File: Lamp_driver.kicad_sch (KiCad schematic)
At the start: 121 parts, among them J302 T44007, J303 T44007, J304 10146581-060_M, J305 T44007, J306 T44007, Q100 MDT7N65, Q301 MPF3N150, Q303 IXYH55N120, Q304 IXYH55N120, Q305 IXYH55N120, U301 IRS2184

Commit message: New placement strategy
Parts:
- R324: footprint Resistor_THT:R_Axial_DIN0617_L17.0mm_D6.0mm_P5.08mm_Vertical -> Resistor_THT:R_Axial_DIN0617_L17.0mm_D6.0mm_P20.32mm_Horizontal
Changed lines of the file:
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@@
 			(justify right bottom)
 		)
-		(property "Netclass" "400V"
+		(property "Netclass" "300V"
 			(at 197.485 172.8555 0)
 			(effects
@@
 			(justify right bottom)
 		)
-		(property "Netclass" "400V"
+		(property "Netclass" "300V"
 			(at 215.9 180.975 0)
 			(effects
@@
 			(justify right bottom)
 		)
-		(property "Netclass" "400V"
+		(property "Netclass" "300V"
 			(at 243.84 180.975 0)
 			(effects
@@
 			(justify right bottom)
 		)
-		(property "Netclass" "400V"
+		(property "Netclass" "300V"
 			(at 255.905 189.23 0)
 			(effects
@@
 			)
 		)
-		(property "Footprint" "Resistor_THT:R_Axial_DIN0617_L17.0mm_D6.0mm_P5.08mm_Vertical"
+		(property "Footprint" "Resistor_THT:R_Axial_DIN0617_L17.0mm_D6.0mm_P20.32mm_Horizontal"
 			(at 250.952 160.02 90)
 			(effects

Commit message: TP placement candidate 90%
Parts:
- R324: footprint Resistor_THT:R_Axial_DIN0617_L17.0mm_D6.0mm_P20.32mm_Horizontal -> Resistor_THT:R_Axial_DIN0617_L17.0mm_D6.0mm_P7.62mm_Vertical
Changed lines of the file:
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@@
 			)
 		)
-		(property "Footprint" "Resistor_THT:R_Axial_DIN0617_L17.0mm_D6.0mm_P20.32mm_Horizontal"
+		(property "Footprint" "Resistor_THT:R_Axial_DIN0617_L17.0mm_D6.0mm_P7.62mm_Vertical"
 			(at 250.952 160.02 90)
 			(effects

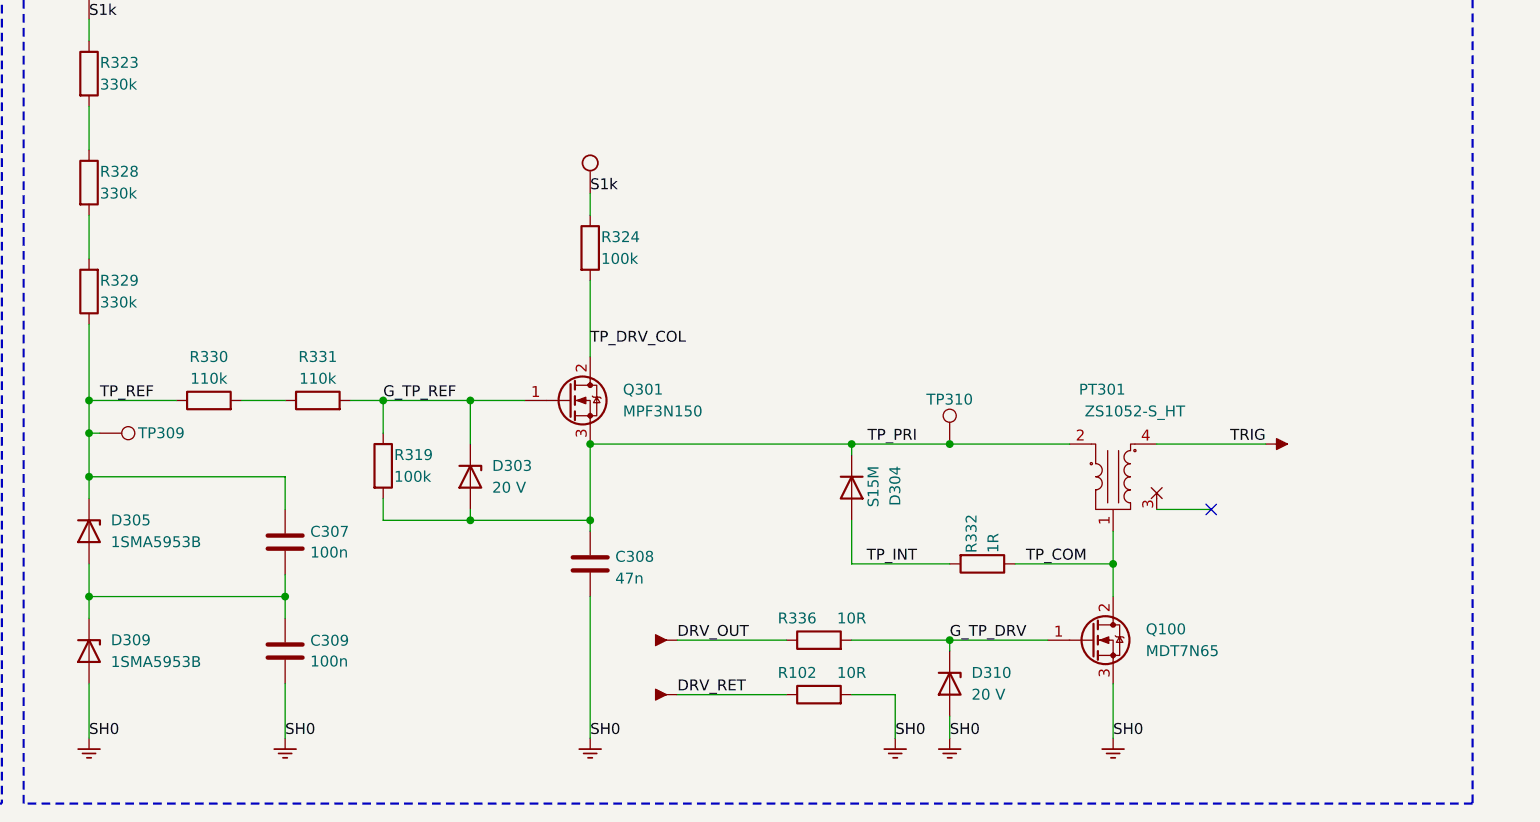
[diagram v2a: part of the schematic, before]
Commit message: Updated some clearance rules
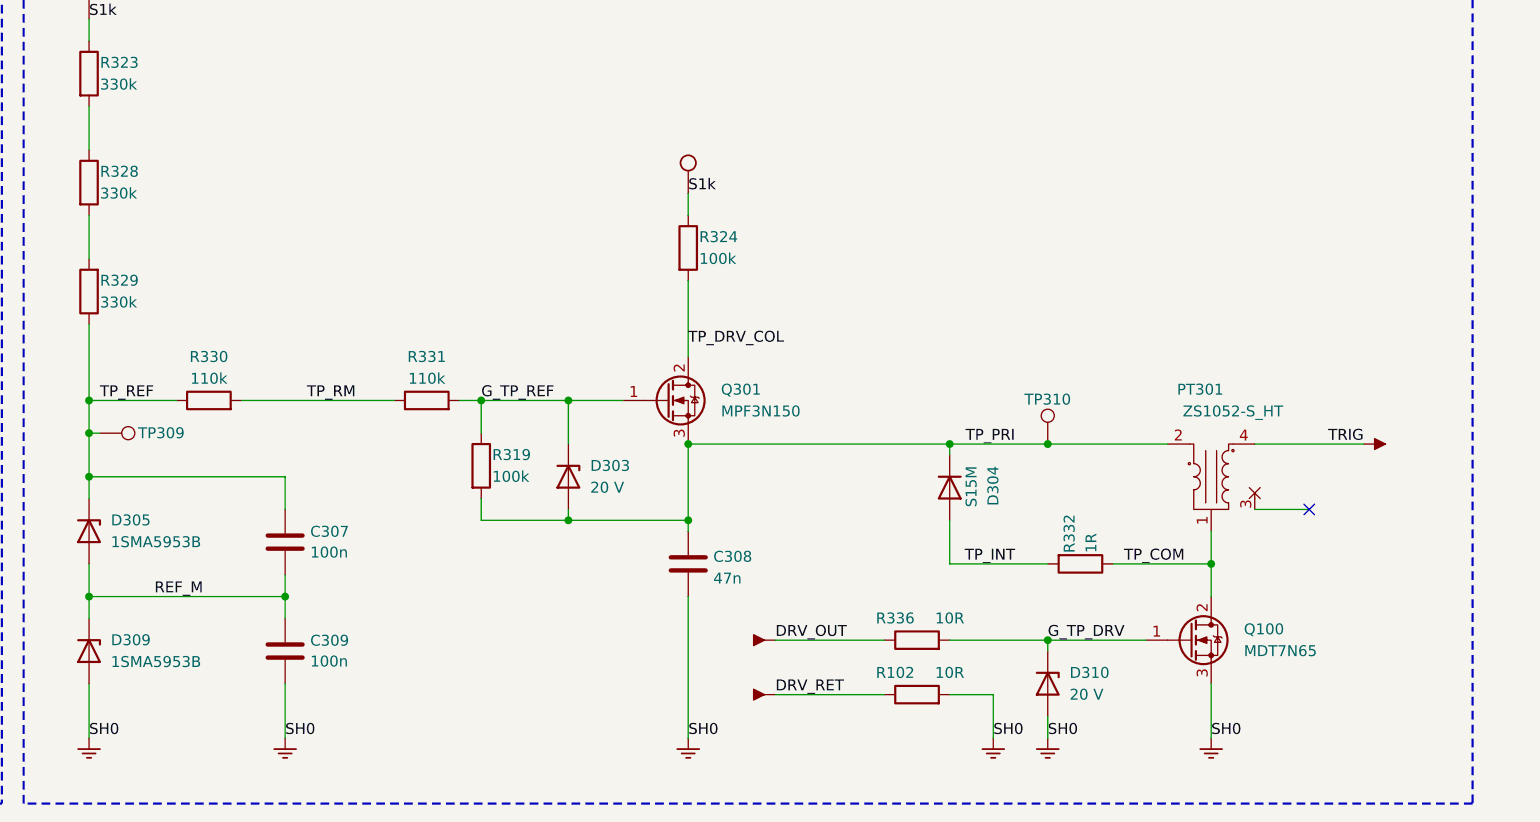
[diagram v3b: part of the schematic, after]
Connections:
- net TP_RM: now reaches R330.2, R331.1
- net REF_M: now reaches C307.2, C309.1, D305.2 (A), D309.1 (K)
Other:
- moved on the sheet: C308, D303, D304, D310, PT301, Q100, Q301, R102, R319, R324, R331, R332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

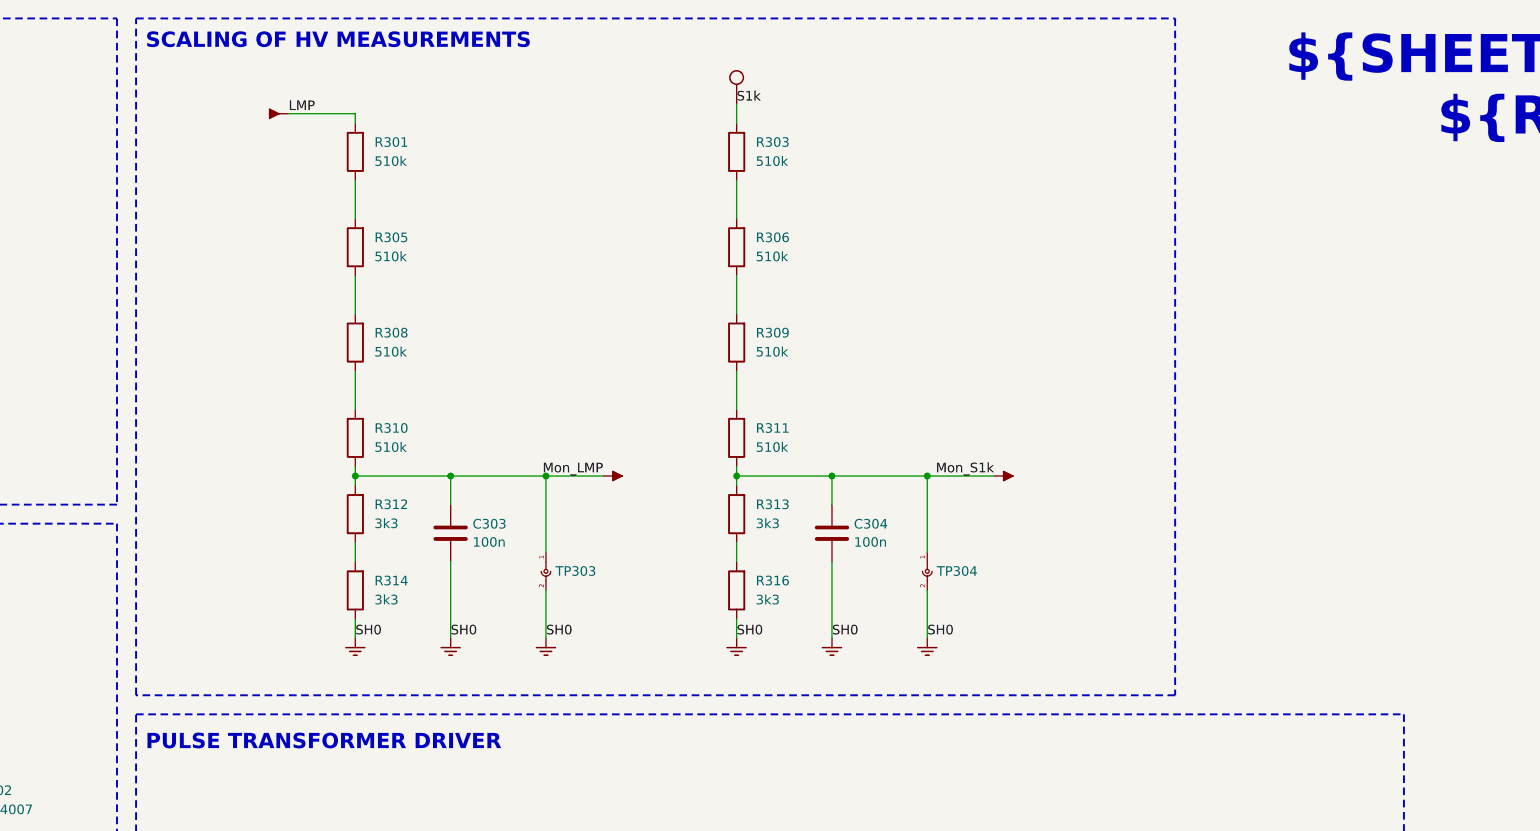
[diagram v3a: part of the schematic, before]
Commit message: Placement complplete, feasibility routing complete
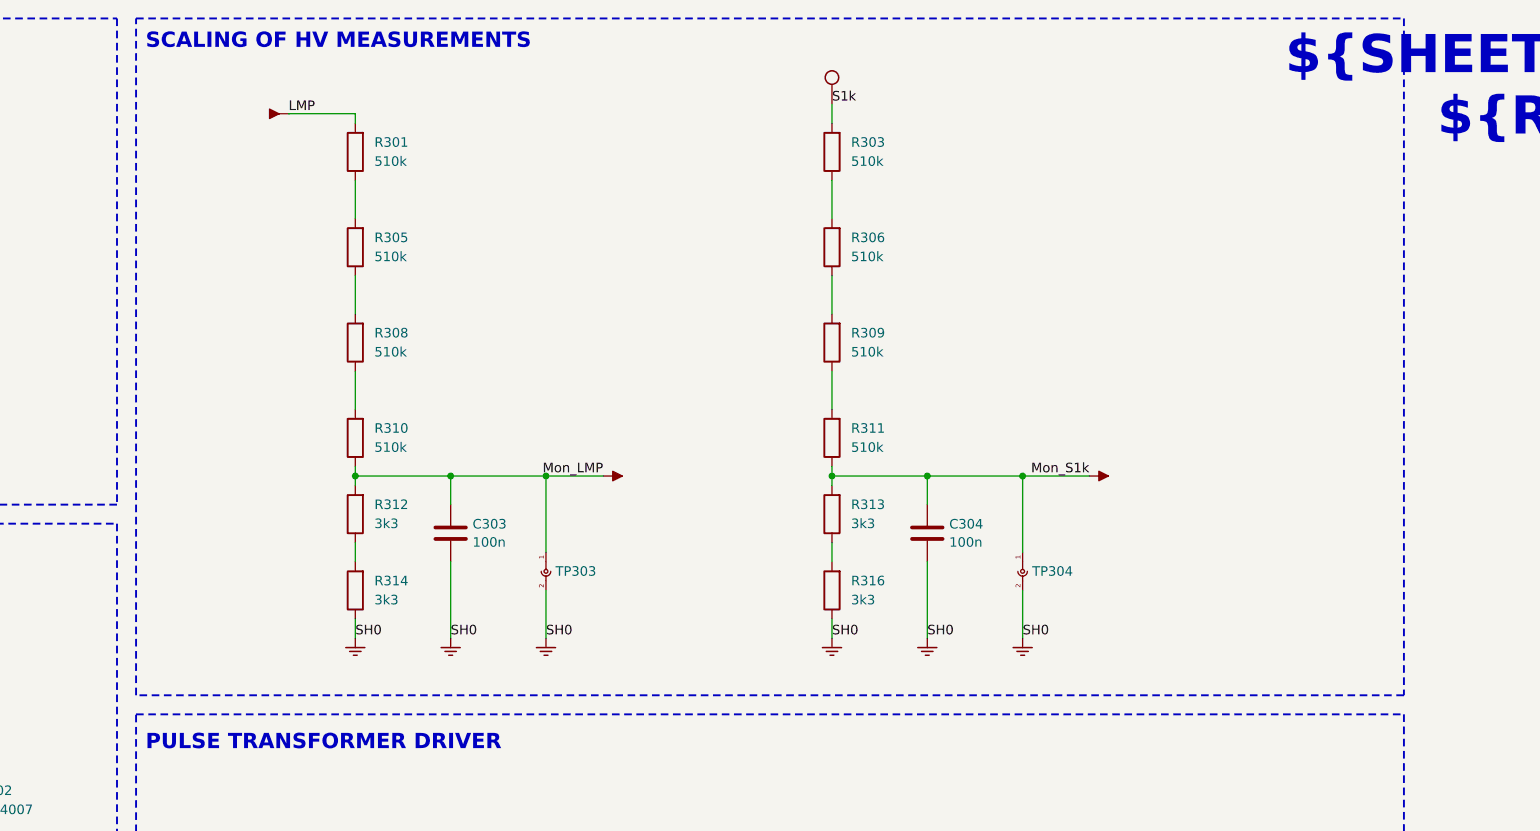
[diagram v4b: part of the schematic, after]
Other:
- moved on the sheet: C304, R303, R306, R309, R311, R313, R316, TP304

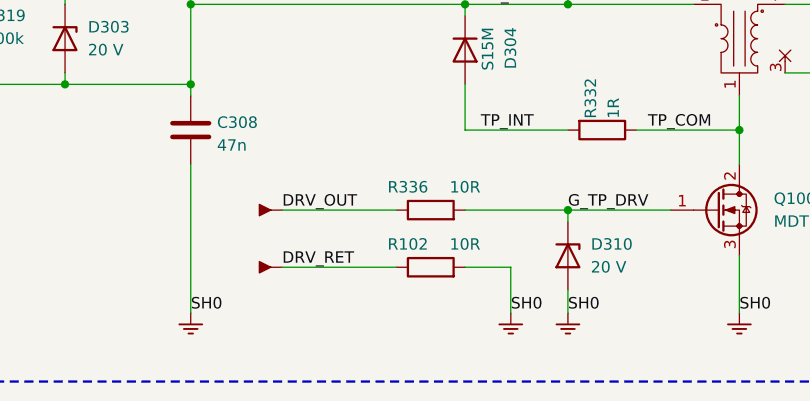
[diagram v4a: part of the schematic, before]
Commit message: Routing complete, silk to do, vias to check, one footprint to update
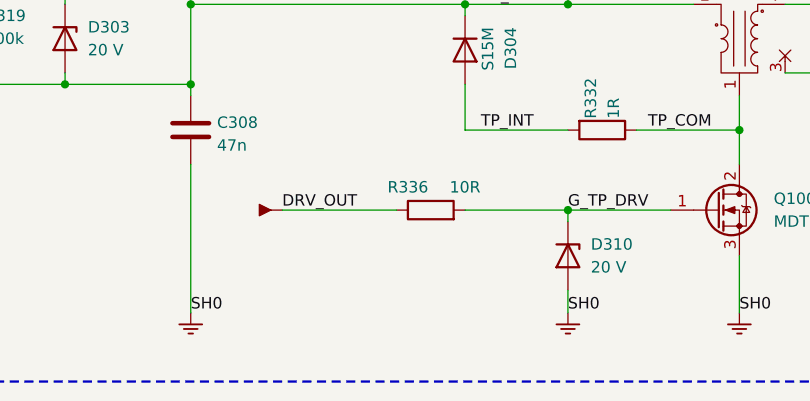
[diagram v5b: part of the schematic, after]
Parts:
- removed P137: ~, symbol personal:Cosmetic_IN
- removed P138: ~, symbol personal:Cosmetic_GND
- removed R102: 10R, Resistor_SMD:R_1206_3216Metric_Pad1.30x1.75mm_HandSolder, symbol Device:R

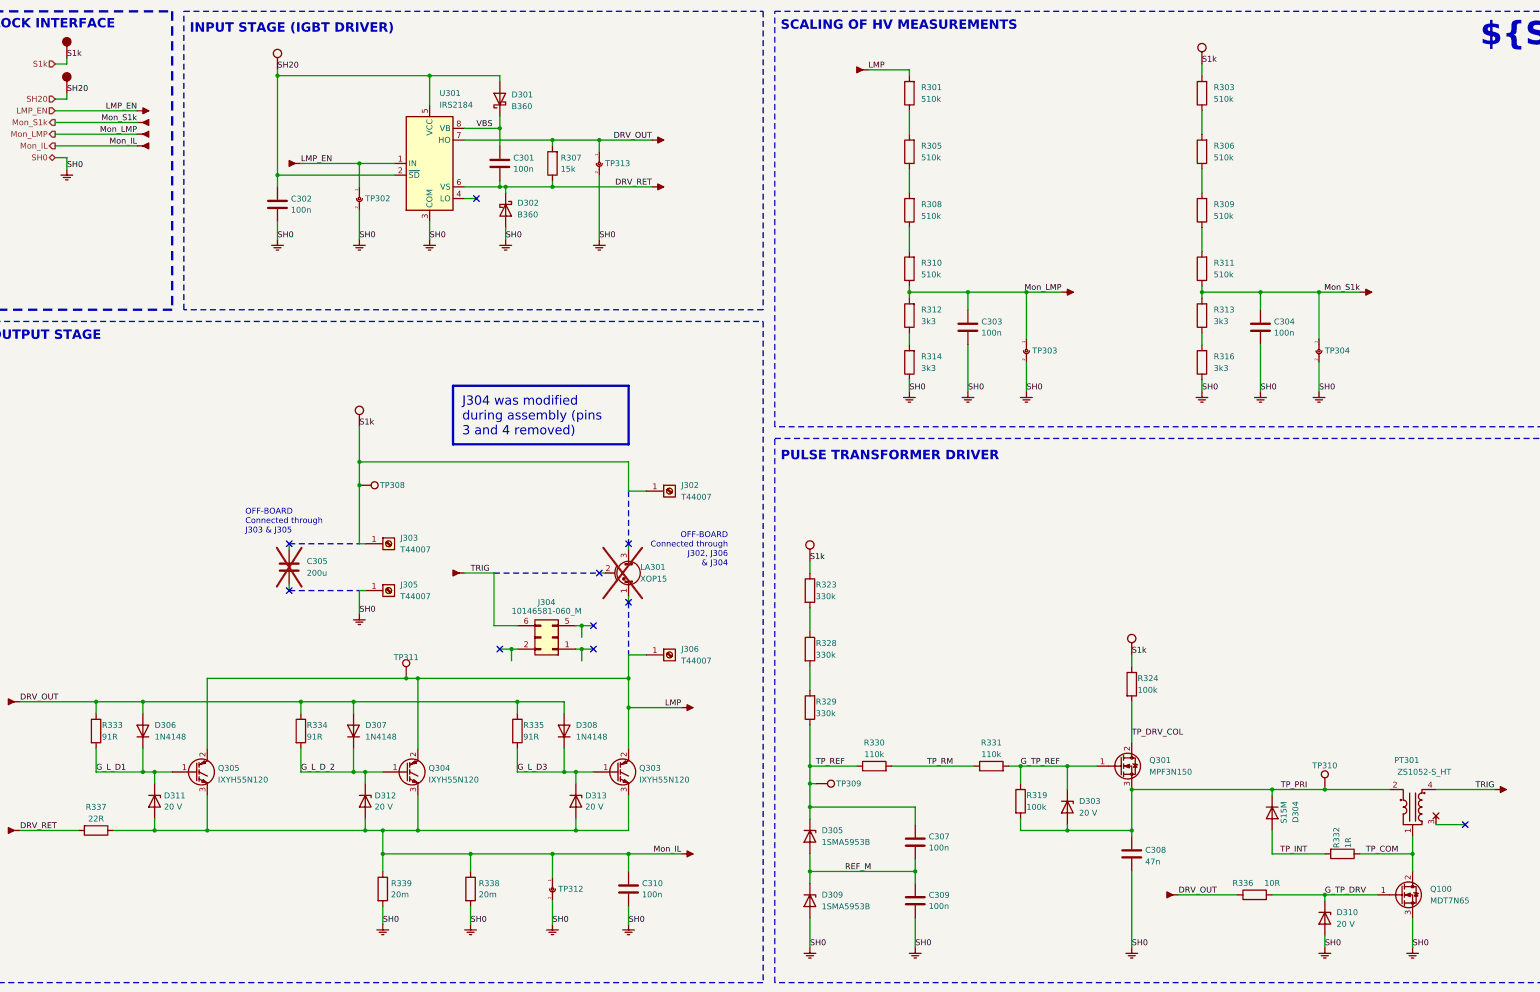
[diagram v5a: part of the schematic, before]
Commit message: Reannotated, silk done, missing some 3D models
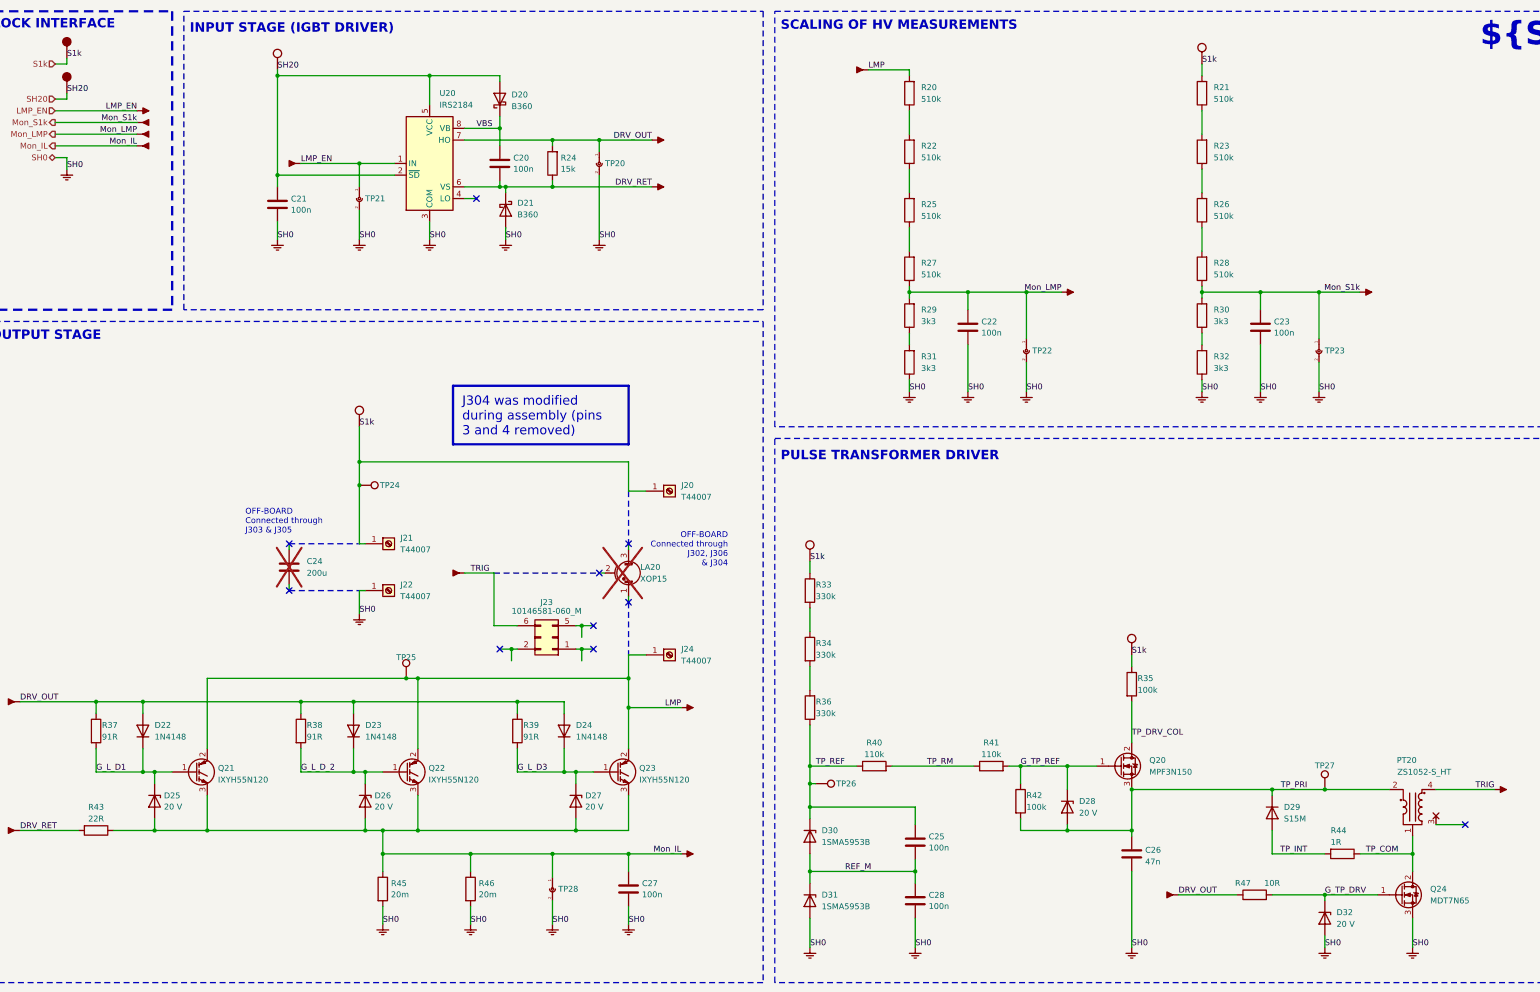
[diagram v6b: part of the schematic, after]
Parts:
- removed Q100: MDT7N65, Package_TO_SOT_SMD:TO-252-2, symbol Transistor_FET:BUZ11
- added Q24: MDT7N65, Package_TO_SOT_SMD:TO-252-2, symbol Transistor_FET:RS9N50D
- Q20: renamed from Q301; footprint Personal:To-220_staggered_2 -> Personal:To-220_staggered_3
- renumbered C301 to C20, C302 to C21, C303 to C22, C304 to C23, C305 to C24, C307 to C25, C308 to C26, C310 to C27, C309 to C28, D301 to D20, D302 to D21, D306 to D22, D307 to D23, D308 to D24, D311 to D25, D312 to D26, D313 to D27, D303 to D28, D304 to D29, D305 to D30, D309 to D31, D310 to D32, J302 to J20, J303 to J21, J305 to J22, J304 to J23, J306 to J24, LA301 to LA20, P378 to P100, P379 to P101, P377 to P102, P370 to P103, P371 to P104, P372 to P105, P373 to P106, P374 to P107, P794 to P62, P305 to P63, P334 to P64, P860 to P65, P795 to P66, P337 to P67, P338 to P68, P858 to P69, P340 to P70, P859 to P71, P342 to P72, P343 to P73, P344 to P74, P347 to P75, P302 to P76, P349 to P77, P350 to P78, P301 to P79, P345 to P80, P346 to P81, P353 to P82, P355 to P83, P303 to P84, P356 to P85, P360 to P86, P304 to P87, P351 to P88, P362 to P89, P864 to P90, P365 to P91, P363 to P92, P863 to P93, P368 to P94, P366 to P95, P862 to P96, P375 to P97, P369 to P98, P3 to P99, PT301 to PT20, Q305 to Q21, Q304 to Q22, Q303 to Q23, R301 to R20, R303 to R21, R305 to R22, R306 to R23, R307 to R24, R308 to R25, R309 to R26, R310 to R27, R311 to R28, R312 to R29, R313 to R30, R314 to R31, R316 to R32, R323 to R33, R328 to R34, R324 to R35, R329 to R36, R333 to R37, R334 to R38, R335 to R39, R330 to R40, R331 to R41, R319 to R42, R337 to R43, R332 to R44, R339 to R45, R338 to R46, R336 to R47, TP313 to TP20, TP302 to TP21, TP303 to TP22, TP304 to TP23, TP308 to TP24, TP311 to TP25, TP309 to TP26, TP310 to TP27, TP312 to TP28, U301 to U20
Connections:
- net G_TP_DRV: now also Q24.1 (G)
- net SH0: now also Q24.3 (S)
- net TP_COM: now also Q24.2 (D)

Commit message: 3D models added
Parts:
- R45, R46: footprint Resistor_SMD:R_Shunt_Vishay_WSR2_WSR3_KelvinConnection -> Personal:R_Shunt_Vishay_WSR2_WSR3_KelvinConnection
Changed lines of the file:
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@@
 			)
 		)
-		(property "Footprint" "Resistor_SMD:R_Shunt_Vishay_WSR2_WSR3_KelvinConnection"
+		(property "Footprint" "Personal:R_Shunt_Vishay_WSR2_WSR3_KelvinConnection"
 			(at 99.822 204.47 90)
 			(effects
@@
 			)
 		)
-		(property "Footprint" "Resistor_SMD:R_Shunt_Vishay_WSR2_WSR3_KelvinConnection"
+		(property "Footprint" "Personal:R_Shunt_Vishay_WSR2_WSR3_KelvinConnection"
 			(at 118.872 204.47 90)
 			(effects

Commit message: Updating mfg layers
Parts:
- removed J23: 10146581-060_M, Personal:Amphenol_Minitek_10146581-060_mod_0, symbol personal:Amphenol_Minitek_10146581-060_mod
- added H20, H21, H22: MountingHole, Personal:Hole_1.0mm, symbol Mechanical:MountingHole
- added J23: Conn_01x03_Pin, Connector_PinHeader_2.54mm:PinHeader_1x03_P2.54mm_Vertical, symbol Connector:Conn_01x03_Pin
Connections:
- net TRIG: now also J23.2 (Pin_2)
- net G_L_D_2 renamed G_L_D2
- no-connect marks 10 -> 9
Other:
- moved on the sheet: C24, J21, J22, TP24
